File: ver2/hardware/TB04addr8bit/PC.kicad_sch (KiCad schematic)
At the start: 2 parts, among them U14 74LS157, U15 74LS157

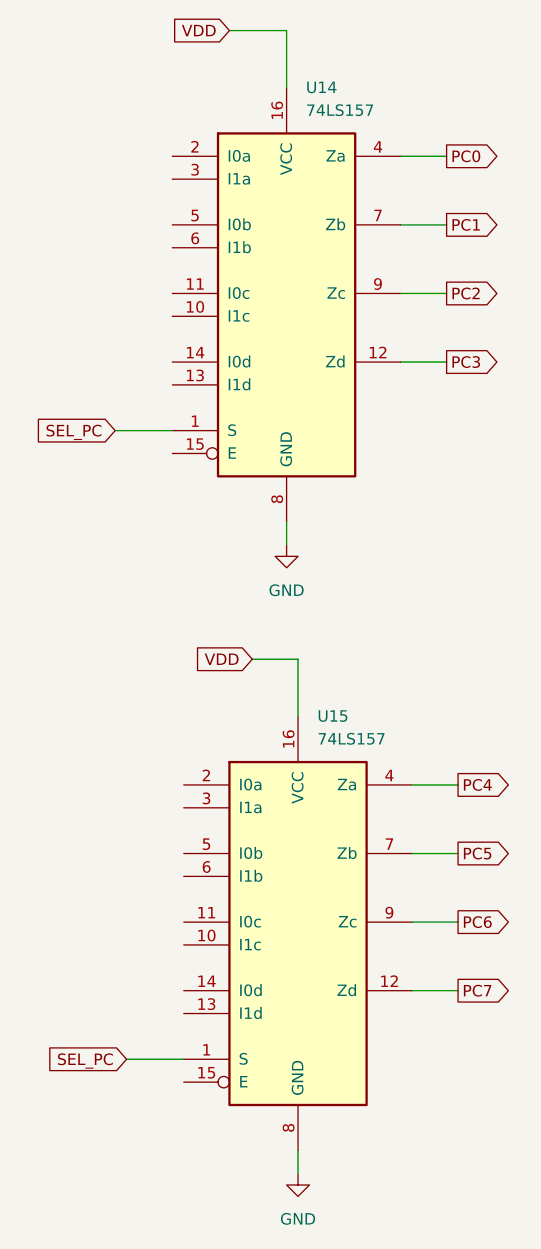
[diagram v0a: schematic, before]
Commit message: ver2: 要修正5件を修正し共通データバス・オペランド源MUX・I/Oを結線
- 6116の/CS極性を修正し、スタック域を含むRAM_STK_SEL(0xC0-0xF7)に統一
- ALU出力をDI0-3へ直結、U21はYドライバ源として残す(LD/POP/RET対策)
- 共通8bitデータバスMD0-7を新設(ROM/RAM/Yドライバ/IN244が排他駆動)
- aポートMUX(74LS253x2)・IN用244・Yドライバ制御ゲートを追加
- IN実行時のROM競合を/OE_ROMに~OE_iAddrを足して回避
- 4bit書込時にMD4-7が浮くのをU17 bank2で0駆動
- 74LS157のEをGND固定、孤立したPC_mAddrシートを削除

Co-Authored-By: Claude Opus 5 <noreply@anthropic.com>
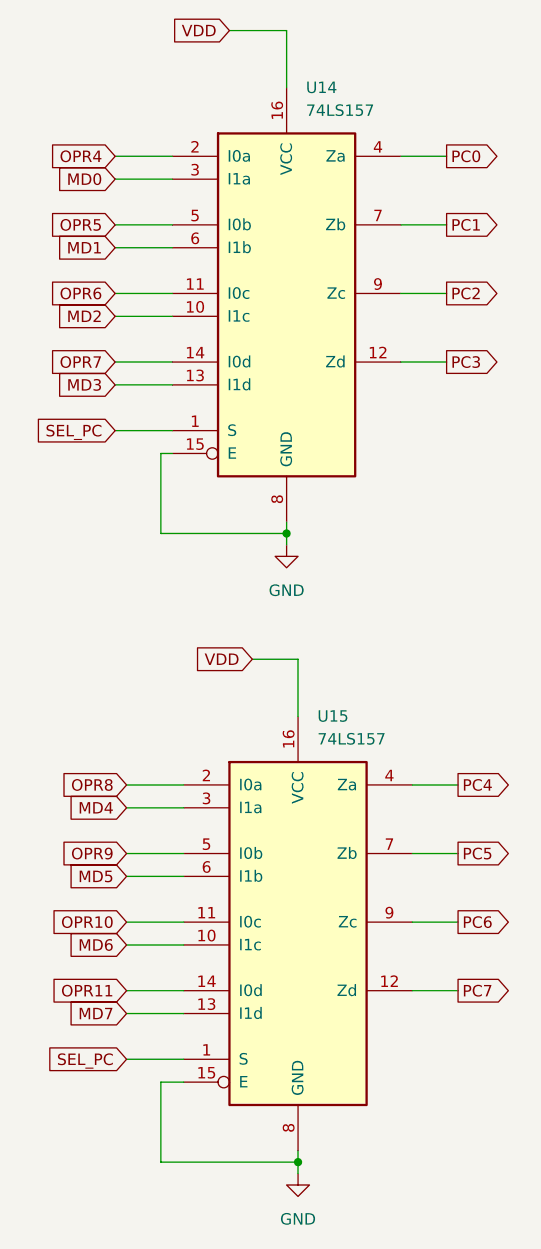
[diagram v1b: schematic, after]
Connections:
- net GND: now also U14.15 (E), U15.15 (E)
- net MD6: now reaches U15.10 (I1c)
- net OPR10: now reaches U15.11 (I0c)
- net MD7: now reaches U15.13 (I1d)
- net OPR11: now reaches U15.14 (I0d)
- net OPR8: now reaches U15.2 (I0a)
- net MD4: now reaches U15.3 (I1a)
- net OPR9: now reaches U15.5 (I0b)
- net MD5: now reaches U15.6 (I1b)
- net MD2: now reaches U14.10 (I1c)
- net OPR6: now reaches U14.11 (I0c)
- net MD3: now reaches U14.13 (I1d)
- net OPR7: now reaches U14.14 (I0d)
- net OPR4: now reaches U14.2 (I0a)
- net MD0: now reaches U14.3 (I1a)
- net OPR5: now reaches U14.5 (I0b)
- net MD1: now reaches U14.6 (I1b)

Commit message: ver2: ゲートICをgatesシートへ集約しアノテーションを掛け直し
- 分散していた8パッケージ(U1/U2/U5/U25/U35/U36/U37/U51)をgatesシートへ集約
- シートをまたぐ11本をグローバルラベル化(~P4/~P5/~OUT_SEL/~CS_RAM/
  ~OE_ROM/CLK_C/CLK_Z/PC_CNT_EN/~PC_PE/~Ena_RS01/~Enb_RS01)
- U40のP2入力がROM_SELに吸着していたのを修正(RAM_SELが逆条件だった)
- !P5の重複インバータを解消、未使用ゲート入力7本をGNDへ
- ALU入力MUXをinPut→PC、PCカウンタをaddrMUX→PCへ移動
- 全体を再アノテーション(シート順採番)。旧→新の対応は電気的変化なしを確認

Co-Authored-By: Claude Opus 5 <noreply@anthropic.com>
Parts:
- added IC401, IC402: 74HC161N, Package_DIP:DIP-16_W7.62mm_Socket, symbol 74HC161:74HC161N
- added U402, U403, U405, U406: 74LS253, Package_DIP:DIP-16_W7.62mm_Socket, symbol 74xx:74LS253
- renumbered U14 to U401, U15 to U404
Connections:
- net GND: now also IC401.8 (GND), IC402.8 (GND), U402.1 (OEa), U402.15 (OEb), U402.8 (GND), U403.1 (OEa), U403.13 (I3b), U403.15 (OEb), U403.3 (I3a), U403.8 (GND), U405.1 (OEa), U405.15 (OEb), U405.8 (GND), U406.1 (OEa), U406.13 (I3b), U406.15 (OEb), U406.3 (I3a), U406.8 (GND)
- net MD0: now also U403.5 (I1a)
- net MD1: now also U403.11 (I1b)
- net MD2: now also U406.5 (I1a)
- net MD3: now also U406.11 (I1b)
- net OPR4: now also U402.3 (I3a), U403.4 (I2a)
- net OPR5: now also U402.13 (I3b), U403.12 (I2b)
- net OPR6: now also U405.3 (I3a), U406.4 (I2a)
- net OPR7: now also U405.13 (I3b), U406.12 (I2b)
- net PC0: now also IC402.3 (D0)
- net PC1: now also IC402.4 (D1)
- net PC2: now also IC402.5 (D2)
- net PC3: now also IC402.6 (D3)
- net PC4: now also IC401.3 (D0)
- net PC5: now also IC401.4 (D1)
- net PC6: now also IC401.5 (D2)
- net PC7: now also IC401.6 (D3)
- net VDD: now also IC401.16 (VCC), IC402.16 (VCC), U402.16 (VCC), U403.16 (VCC), U405.16 (VCC), U406.16 (VCC)
- new net: IC401.10 (CET), IC402.15 (TC)
- new net CLK_CPU: IC401.2 (CP), IC402.2 (CP)
- new net DOa0: U402.5 (I1a), U402.6 (I0a)
- new net DOa1: U402.10 (I0b), U402.11 (I1b)
- new net DOa2: U405.5 (I1a), U405.6 (I0a)
- new net DOa3: U405.10 (I0b), U405.11 (I1b)
- new net DOb0: U403.6 (I0a)
- new net DOb1: U403.10 (I0b)
- new net DOb2: U406.6 (I0a)
- new net DOb3: U406.10 (I0b)
- new net OPR0: U402.4 (I2a)
- new net OPR1: U402.12 (I2b)
- new net OPR2: U405.4 (I2a)
- new net OPR3: U405.12 (I2b)
- new net PC_CNT_EN: IC401.7 (CEP), IC402.10 (CET), IC402.7 (CEP)
- new net PC_Q0: IC402.14 (Q0)
- new net PC_Q1: IC402.13 (Q1)
- new net PC_Q2: IC402.12 (Q2)
- new net PC_Q3: IC402.11 (Q3)
- new net PC_Q4: IC401.14 (Q0)
- new net PC_Q5: IC401.13 (Q1)
- new net PC_Q6: IC401.12 (Q2)
- new net PC_Q7: IC401.11 (Q3)
- new net SEL_A: U402.2 (A1), U405.2 (A1)
- new net SEL_B0: U403.14 (A0), U406.14 (A0)
- new net SEL_B1: U403.2 (A1), U406.2 (A1)
- new net SEL_IMM: U402.14 (A0), U405.14 (A0)
- new net alu_a0: U402.7 (Za)
- new net alu_a1: U402.9 (Zb)
- new net alu_a2: U405.7 (Za)
- new net alu_a3: U405.9 (Zb)
- new net alu_b0: U403.7 (Za)
- new net alu_b1: U403.9 (Zb)
- new net alu_b2: U406.7 (Za)
- new net alu_b3: U406.9 (Zb)
- new net ~{PC_PE}: IC401.9 (~PE), IC402.9 (~PE)
- new net ~{RST}: IC401.1 (~MR), IC402.1 (~MR)
- no-connect marks 0 -> 1
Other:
- note added: "PC_H"
- note added: "PC_L"
- note added: "mAddrH"
- moved on the sheet: U401, U404

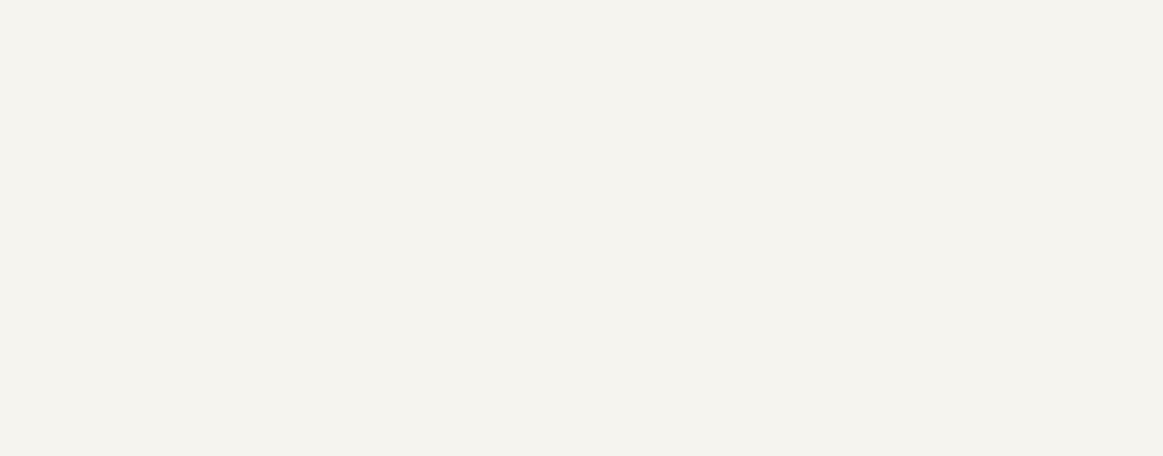
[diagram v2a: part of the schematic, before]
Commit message: ver2: I/Oを4ch化しアドレスバスの浮きを解消(OUTは377化・RAMのCSをEXEゲート)
- I/Oアドレス源244・port位置MUX157・portデコード139を追加し、IN244×4/OUT×4に拡張。
  IN/OUT実行中も 0xF8|port / 0xFC|port をアドレスバスへ出すことで、全相・全命令で
  アドレスバスが必ず1つに駆動される状態にした(OUTのRAM誤書込・INのMD衝突を構造的に解消)。
- OUTポートを74HC273→74HC377へ。~E=139出力・CP=~CLK_CPUとし、クロックゲートなしで
  EXE中間の1回だけ取り込む(取り込み余裕が15ns→半相)。
- ~CS_RAM を !(RAM_STK_SEL & EXE) に変更(CS_RAMノード新設)。EXE末に出る第2の書込パルスを
  約38nsに短縮しtWP未満に収めた。フェッチ3相でRAMが非選択になる副次効果あり。
- OUTコネクタのピン配列を7segIF J1に合わせて入れ替え(D3出力がVDDへ短絡する組合せを回避)。
- パスコンが無かった2シート(outPort・PC_aluMux)に追加。RS.kicad_sch を RS00.kicad_sch へ改名。

Co-Authored-By: Claude Opus 5 <noreply@anthropic.com>
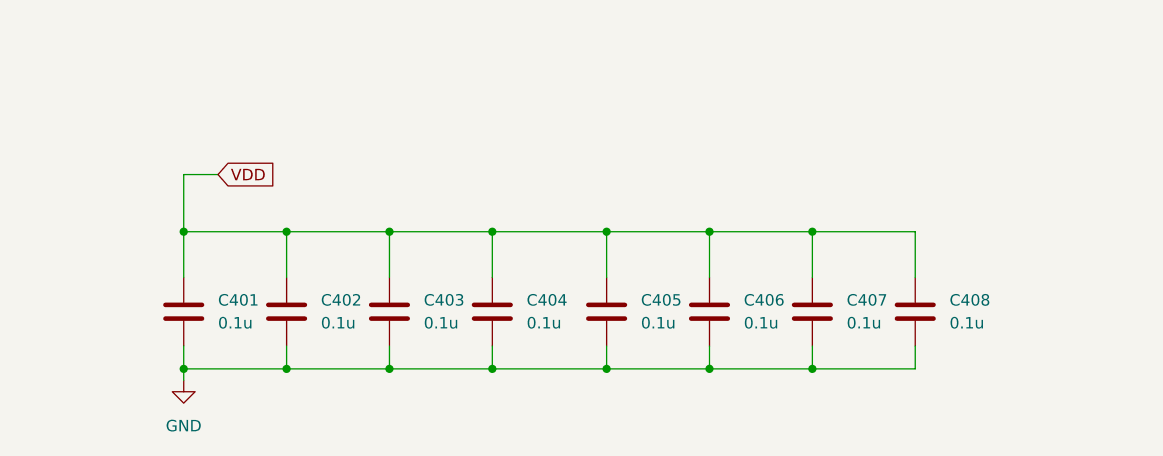
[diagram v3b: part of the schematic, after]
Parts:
- added C401, C402, C403, C404, C405, C406, C407, C408: 0.1u, symbol Device:C
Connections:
- net GND: now also C401.1, C402.1, C403.1, C404.1, C405.1, C406.1, C407.1, C408.1
- net VDD: now also C401.2, C402.2, C403.2, C404.2, C405.2, C406.2, C407.2, C408.2
